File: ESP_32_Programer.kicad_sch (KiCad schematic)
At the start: 18 parts, among them J1 TYPE-C 16PIN 2MD(073), J2 Conn_01x06, Q1 SS8050, Q2 SS8050, U1 CP2102N-A02-GQFN28R

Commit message: completando el diseño de la pcb
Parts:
- added C1, C2: 1uF, Capacitor_SMD:C_0805_2012Metric, symbol kmr:C_1uF_0805
- added U2: AP2112K-3.3, Package_TO_SOT_SMD:SC-74A-5_1.55x2.9mm_P0.95mm, symbol Regulator_Linear:AP2112K-3.3
- J2: symbol Connector_Generic:Conn_01x06 -> Connector_Generic:Conn_02x03_Odd_Even
- R3: symbol Device:R_US -> kmr:R_22.1k_0603; IPN (none) -> RES-000105-00; InvenTree (none) -> 105; Part URL (none) -> http://200.234.232.238:8080/part/105/; Temperature Range (none) -> -55℃~+155℃; Tolerance (none) -> ±1%
- R4: symbol Device:R_US -> kmr:R_47.5k_0603; IPN (none) -> RES-000107-00; InvenTree (none) -> 107; Part URL (none) -> http://200.234.232.238:8080/part/107/; Temperature Range (none) -> -55℃~+155℃; Tolerance (none) -> ±1%
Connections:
- net +3V3: now also J2.2 (Pin_2), C2.1, U2.5 (VOUT); no longer J2.1 (Pin_1)
- net EN: now also J2.1 (Pin_1); no longer J2.4 (Pin_4)
- net GND: now also J1.S1 (SHIELD), J2.4 (Pin_4), C1.2, C2.2, U2.2 (GND); no longer J2.6 (Pin_6)
- net IO0: now also J2.6 (Pin_6); no longer J2.5 (Pin_5)
- net RX: now also J2.5 (Pin_5); no longer J2.2 (Pin_2)
- net VBUS: now also C1.1, U2.1 (VIN), U2.3 (EN)
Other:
- note added: "https://www.circuitstate.com/pinouts/espressif-esp-prog-esp32-jtag-debug-probe-pinout-diagram/"
- moved on the sheet: J2

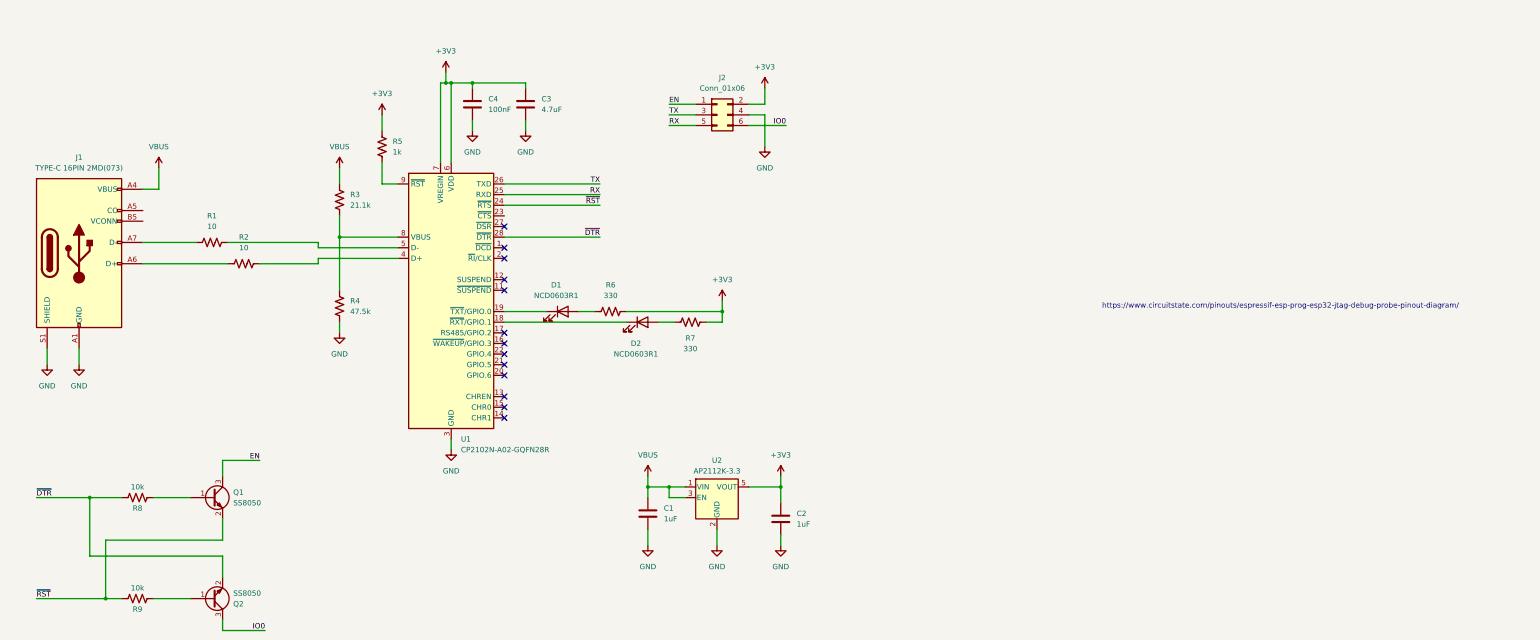
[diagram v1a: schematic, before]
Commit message: corrigiendo error en USB y completando BOM
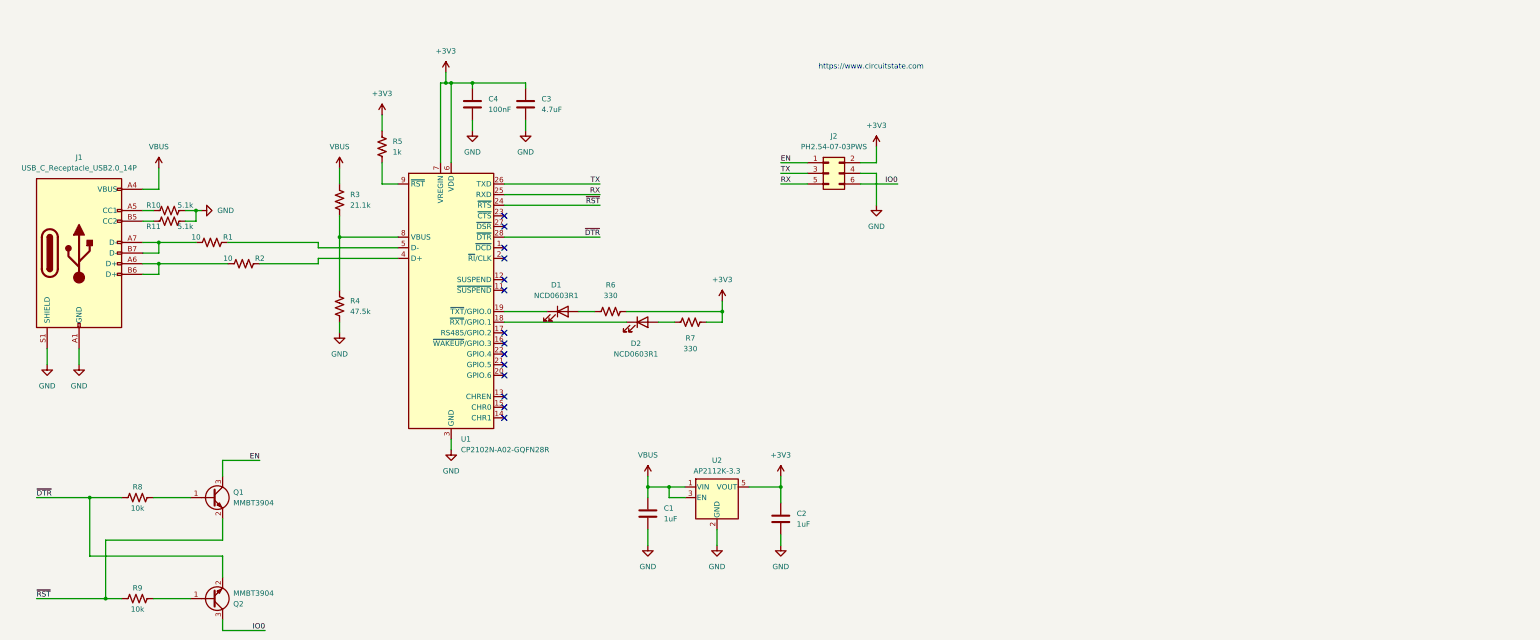
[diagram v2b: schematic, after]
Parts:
- removed Q2: SS8050, Package_TO_SOT_SMD:SOT-23, symbol Device:Q_NPN_BEC
- removed R9: 10k, Resistor_SMD:R_0603_1608Metric_Pad0.98x0.95mm_HandSolder, symbol Device:R_US
- added Q2: MMBT3904, Package_TO_SOT_SMD:SOT-23, symbol kmr:MMBT3904 RFG
- added R10, R11: 5.1k, Resistor_SMD:R_0603_1608Metric, symbol kmr:R_5.1k_0603
- added R9: 10k, Resistor_SMD:R_0603_1608Metric, symbol kmr:R_10k_0603
- C1, C2: LCSC (none) -> C28323
- C3: LCSC (none) -> C1705
- C4: LCSC (none) -> C14663
- D1, D2: LCSC (none) -> C84263
- J1: value TYPE-C 16PIN 2MD(073) -> USB_C_Receptacle_USB2.0_14P; symbol kmr:CON_USB_3.1 -> Connector:USB_C_Receptacle_USB2.0_14P; LCSC (none) -> C2765186
- J2: value Conn_01x06 -> PH2.54-07-03PWS; LCSC (none) -> C7501617; Manufacturer (none) -> XUNPU; Part # (none) -> PH2.54-07-03PWS; Price (none) -> 0.0390
- Q1: value SS8050 -> MMBT3904; symbol Device:Q_NPN_BEC -> kmr:MMBT3904 RFG; IPN (none) -> TRA-000142-00; InvenTree (none) -> 142; LCSC (none) -> C727127; LCSC Part C164885 -> (none); Manufacturer Jiangsu Changjing Electronics Technology Co. -> TWGMC; Mfr. Part SS8050-G -> (none); Part # (none) -> MMBT3904; Part URL (none) -> http://200.234.232.238:8080/part/142/
- R1, R2: LCSC (none) -> C22859
- R3: LCSC (none) -> C137768
- R4: LCSC (none) -> C137715
- R5: IPN RES-000159-00 -> RES-000158-00; InvenTree 159 -> 158; LCSC (none) -> C217840; Part URL http://200.234.232.238:8080/part/159/ -> http://200.234.232.238:8080/part/158/
- R6, R7: LCSC (none) -> C105881
- R8: footprint Resistor_SMD:R_0603_1608Metric_Pad0.98x0.95mm_HandSolder -> Resistor_SMD:R_0603_1608Metric; symbol Device:R_US -> kmr:R_10k_0603; IPN (none) -> RES-000039-00; LCSC (none) -> C323556; LCSC Part C25804 -> (none); Manufacturer UNI-ROYAL(Uniroyal Elec) -> KAMAYA; Mfr. Part 0603WAF1002T5E -> (none); Part # (none) -> RMC16K103FTP; Part URL (none) -> http://200.234.232.238:8080/part/39/; Tolerance (none) -> ±1%
- U1: LCSC (none) -> C964632
- U2: LCSC (none) -> C51118; Manufacturer (none) -> Diodes Incorporated; Part # (none) -> AP2112K-3.3TRG1; Price (none) -> 0.109
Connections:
- net GND: now also R10.2, R11.2
- net IO0: now also Q2.3 (C)
- net ~{DTR}: now also Q2.2 (E)
- net ~{RST}: now also R9.1
- net at J1.A7 (D-), R1.1: now also J1.B7 (D-)
- net at J1.A5 (CC1): now also R10.1
- net at J1.A6 (D+), R2.1: now also J1.B6 (D+)
- net at J1.B5 (CC2): now also R11.1
- new net: Q2.1 (B), R9.2
- no-connect marks 13 -> 14
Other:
- note added: "https://www.circuitstate.com"
- note removed: "https://www.circuitstate.com/pinouts/espressif-esp-prog-esp32-jtag-debug-probe-pinout-diagram/"
- moved on the sheet: J2

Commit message: actualizando documentacion generando version v1.1.0
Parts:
- C1, C2: Manufacturer (none) -> Samsung Electro-Mechanics; Part # (none) -> CL21B105KBFNNNE
- C3: Manufacturer (none) -> Samsung Electro-Mechanics; Part # (none) -> CL10A475KP8NNNC
- C4: Manufacturer (none) -> YAGEO; Part # (none) -> CC0603KRX7R9BB104
- D1, D2: Manufacturer (none) -> NATIONSTAR; Part # (none) -> NCD0603R1
- J1: Manufacturer (none) -> SHOU HAN; Part # (none) -> TYPE-C 16PIN 2MD(073)
- R1, R2: Manufacturer (none) -> UNI-ROYAL; Part # (none) -> 0603WAF100JT5E
- R10, R11: Manufacturer (none) -> UNI-ROYAL; Part # (none) -> 0603WAF5101T5E
- R3: Manufacturer (none) -> YAGEO; Part # (none) -> RC0603FR-0722K1L
- R4: Manufacturer (none) -> YAGEO; Part # (none) -> RC0603FR-0747K5L
- R5: Manufacturer (none) -> Viking; Part # (none) -> ARG03FTC1001
- R6, R7: Manufacturer (none) -> YAGEO; Part # (none) -> RC0603FR-07330RL
- U1: Manufacturer (none) -> SILICON LABS; Part # (none) -> CP2102N-A02-GQFN28R
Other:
- title: ESP32_programer -> ESP32_prog_lite
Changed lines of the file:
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@@
 	(paper "A4")
 	(title_block
-		(title "ESP32_programer")
+		(title "ESP32_prog_lite")
 		(date "2025-06-17")
-		(rev "v1.0.0")
+		(rev "v1.1.0")
 	)
 	(text "https://www.circuitstate.com"
@@
 			)
 		)
-		(property "Part #" ""
+		(property "Part #" "0603WAF100JT5E"
 			(at 82.55 86.36 0)
 			(effects
@@
 			)
 		)
-		(property "Manufacturer" ""
+		(property "Manufacturer" "UNI-ROYAL"
 			(at 82.55 86.36 0)
 			(effects
@@
 			)
 		)
-		(property "Part #" ""
+		(property "Part #" "RC0603FR-07330RL"
 			(at 196.85 105.41 0)
 			(effects
@@
 			)
 		)
-		(property "Manufacturer" ""
+		(property "Manufacturer" "YAGEO"
 			(at 196.85 105.41 0)
 			(effects
@@
 			)
 		)
-		(property "Part #" ""
+		(property "Part #" "RC0603FR-07330RL"
 			(at 177.8 102.87 0)
 			(effects
@@
 			)
 		)
-		(property "Manufacturer" ""
+		(property "Manufacturer" "YAGEO"
 			(at 177.8 102.87 0)
 			(effects
@@
 			)
 		)
-		(property "Part #" ""
+		(property "Part #" "CL10A475KP8NNNC"
 			(at 157.48 53.34 0)
 			(effects
@@
 			)
 		)
-		(property "Manufacturer" ""
+		(property "Manufacturer" "Samsung Electro-Mechanics"
 			(at 157.48 53.34 0)
 			(effects
@@
 			)
 		)
-		(property "Part #" ""
+		(property "Part #" "NCD0603R1"
 			(at 185.42 105.41 0)
 			(effects
@@
 			)
 		)
-		(property "Manufacturer" ""
+		(property "Manufacturer" "NATIONSTAR"
 			(at 185.42 105.41 0)
 			(effects
@@
 			)
 		)
-		(property "Part #" ""
+		(property "Part #" "NCD0603R1"
 			(at 166.37 102.87 0)
 			(effects
@@
 			)
 		)
-		(property "Manufacturer" ""
+		(property "Manufacturer" "NATIONSTAR"
 			(at 166.37 102.87 0)
 			(effects
@@
 			)
 		)
-		(property "Part #" ""
+		(property "Part #" "CC0603KRX7R9BB104"
 			(at 144.78 53.34 0)
 			(effects
@@
 			)
 		)
-		(property "Manufacturer" ""
+		(property "Manufacturer" "YAGEO"
 			(at 144.78 53.34 0)
 			(effects
@@
 			)
 		)
-		(property "Part #" ""
+		(property "Part #" "RC0603FR-0747K5L"
 			(at 113.03 101.6 0)
 			(effects
@@
 			)
 		)
-		(property "Manufacturer" ""
+		(property "Manufacturer" "YAGEO"
 			(at 113.03 101.6 0)
 			(effects
@@
 			)
 		)
-		(property "Part #" ""
+		(property "Part #" "TYPE-C 16PIN 2MD(073)"
 			(at 50.8 88.9 0)
 			(effects
@@
 			)
 		)
-		(property "Manufacturer" ""
+		(property "Manufacturer" "SHOU HAN"
 			(at 50.8 88.9 0)
 			(effects
@@
 			)
 		)
-		(property "Part #" ""
+		(property "Part #" "CL21B105KBFNNNE"
 			(at 218.44 152.4 0)
 			(effects
@@
 			)
 		)
-		(property "Manufacturer" ""
+		(property "Manufacturer" "Samsung Electro-Mechanics"
 			(at 218.44 152.4 0)
 			(effects
@@
 			)
 		)
-		(property "Part #" ""
+		(property "Part #" "0603WAF5101T5E"
 			(at 72.39 81.28 0)
 			(effects
@@
 			)
 		)
-		(property "Manufacturer" ""
+		(property "Manufacturer" "UNI-ROYAL"
 			(at 72.39 81.28 0)
 			(effects
@@
 			)
 		)
+		(property "Part #" "0603WAF100JT5E"
+			(at 90.17 91.44 90)
+			(effects
+				(font
+					(size 1.27 1.27)
+				)
+				(hide yes)
+			)
+		)
+		(property "Manufacturer" "UNI-ROYAL"
+			(at 90.17 91.44 90)
+			(effects
+				(font
+					(size 1.27 1.27)
+				)
+				(hide yes)
+			)
+		)
 		(pin "2"
 		)
@@
 			)
 		)
-		(property "Part #" ""
+		(property "Part #" "0603WAF5101T5E"
 			(at 72.39 78.74 0)
 			(effects
@@
 			)
 		)
-		(property "Manufacturer" ""
+		(property "Manufacturer" "UNI-ROYAL"
 			(at 72.39 78.74 0)
 			(effects
@@
 			)
 		)
-		(property "Part #" ""
+		(property "Part #" "CL21B105KBFNNNE"
 			(at 186.69 151.13 0)
 			(effects
@@
 			)
 		)
-		(property "Manufacturer" ""
+		(property "Manufacturer" "Samsung Electro-Mechanics"
 			(at 186.69 151.13 0)
 			(effects
@@
 			)
 		)
-		(property "Part #" ""
+		(property "Part #" "RC0603FR-0722K1L"
 			(at 113.03 76.2 0)
 			(effects
@@
 			)
 		)
-		(property "Manufacturer" ""
+		(property "Manufacturer" "YAGEO"
 			(at 113.03 76.2 0)
 			(effects
@@
 			)
 		)
-		(property "Part #" ""
+		(property "Part #" "ARG03FTC1001"
 			(at 123.19 63.5 0)
 			(effects
@@
 			)
 		)
-		(property "Manufacturer" ""
+		(property "Manufacturer" "Viking"
 			(at 123.19 63.5 0)
 			(effects
@@
 			)
 		)
-		(property "Part #" ""
+		(property "Part #" "CP2102N-A02-GQFN28R"
 			(at 139.7 100.33 0)
 			(effects
@@
 			)
 		)
-		(property "Manufacturer" ""
+		(property "Manufacturer" "SILICON LABS"
 			(at 139.7 100.33 0)
 			(effects
